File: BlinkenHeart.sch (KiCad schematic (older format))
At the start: 21 parts, among them IC1 ATTINY85-S, P1 CONN_01X06, SW1 SW_Push, SW2 SW_DPDT_x2

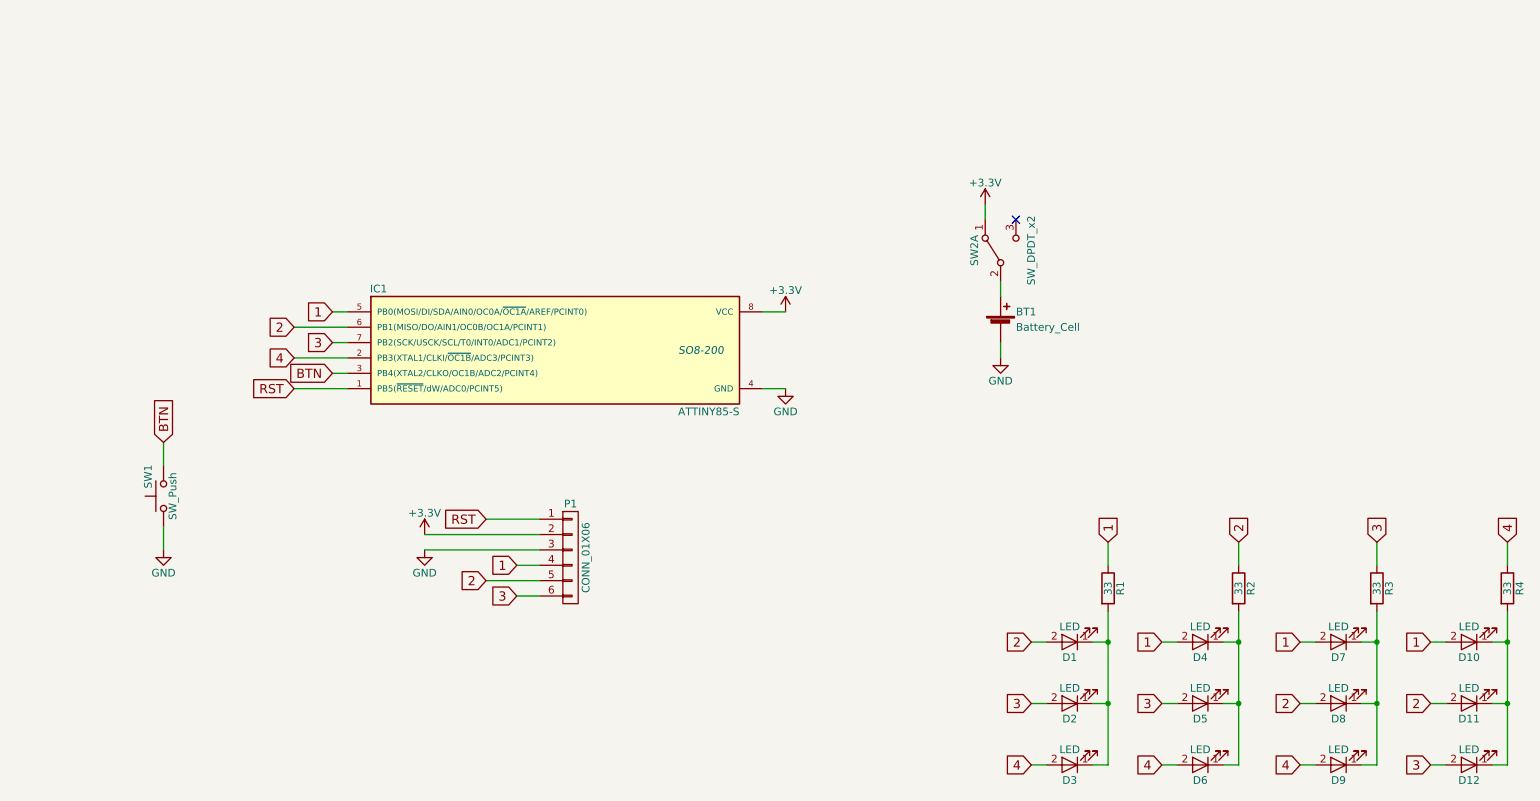
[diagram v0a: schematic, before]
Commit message: Did some refactoring of the schematic. Ordered the ICSP Pins. Added a VCC Capacitor and an Reset-Pull-Up-Resisor
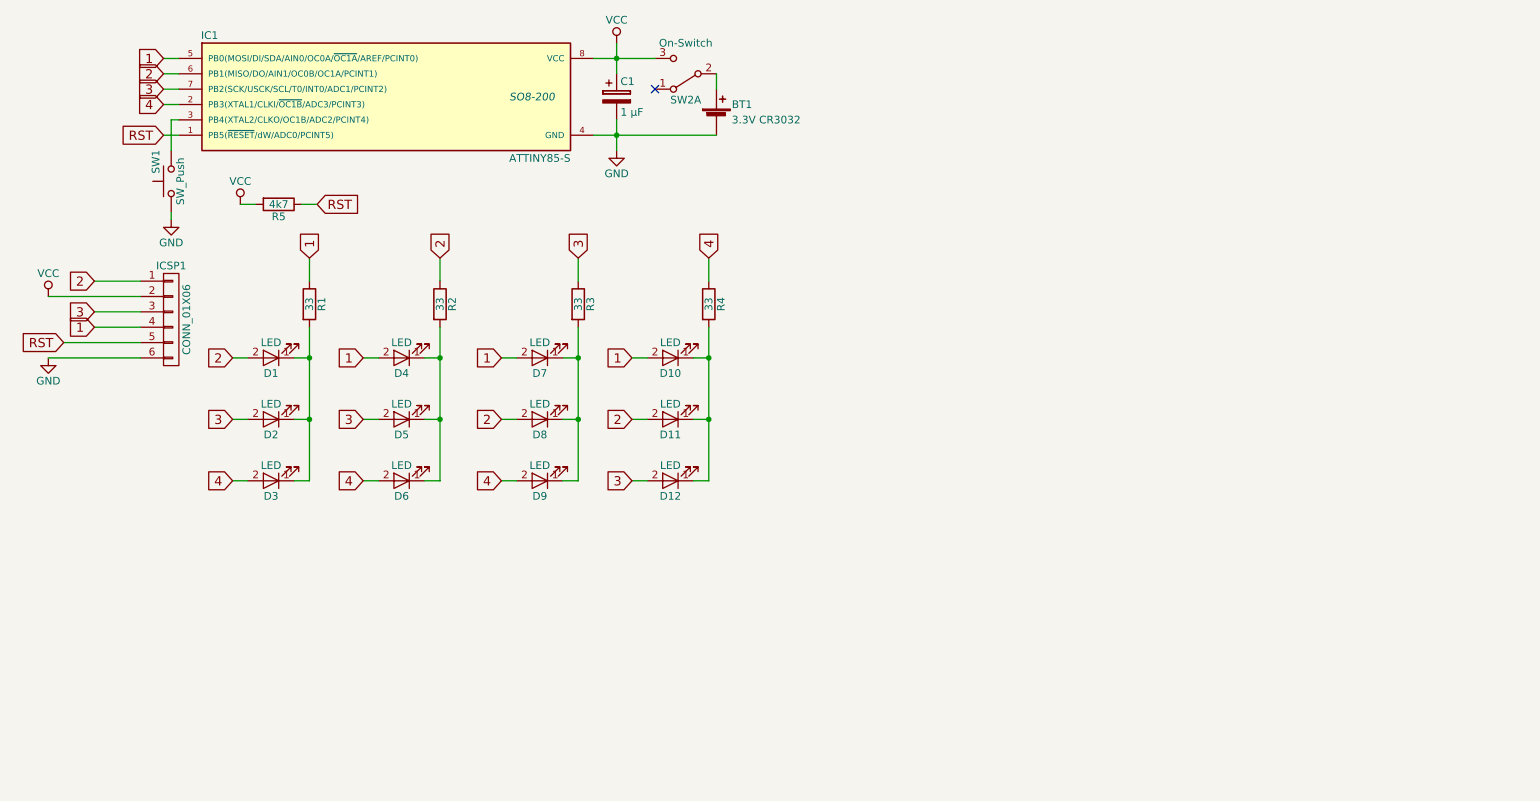
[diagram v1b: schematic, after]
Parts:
- added C1: 1 μF, symbol CP
- added R5: 4k7, symbol R
- BT1: value Battery_Cell -> 3.3V CR3032
- SW2: value SW_DPDT_x2 -> On-Switch
- renumbered P1 to ICSP1
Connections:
- net 2: now also ICSP1.1 (P1); no longer ICSP1.5 (P5)
- net 3: now also ICSP1.3 (P3); no longer ICSP1.6 (P6)
- net GND: now also ICSP1.6 (P6), C1.2; no longer ICSP1.3 (P3)
- net RST: now also ICSP1.5 (P5), R5.1; no longer ICSP1.1 (P1)
- net VCC: now reaches SW2.3 (C)
- net VCC: now also IC1.8 (VCC), ICSP1.2 (P2), C1.1, R5.2
- removed net +3V3: IC1.8 (VCC), ICSP1.2 (P2), SW2.1 (A)
- net BTN: no longer names the net of IC1.3 (PB4(XTAL2/CLKO/OC1B/ADC2/PCINT4)), SW1.2
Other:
- moved on the sheet: BT1, D1, D10, D11, D12, D2, D3, D4, D5, D6, D7, D8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

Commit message: assigned missing footprints
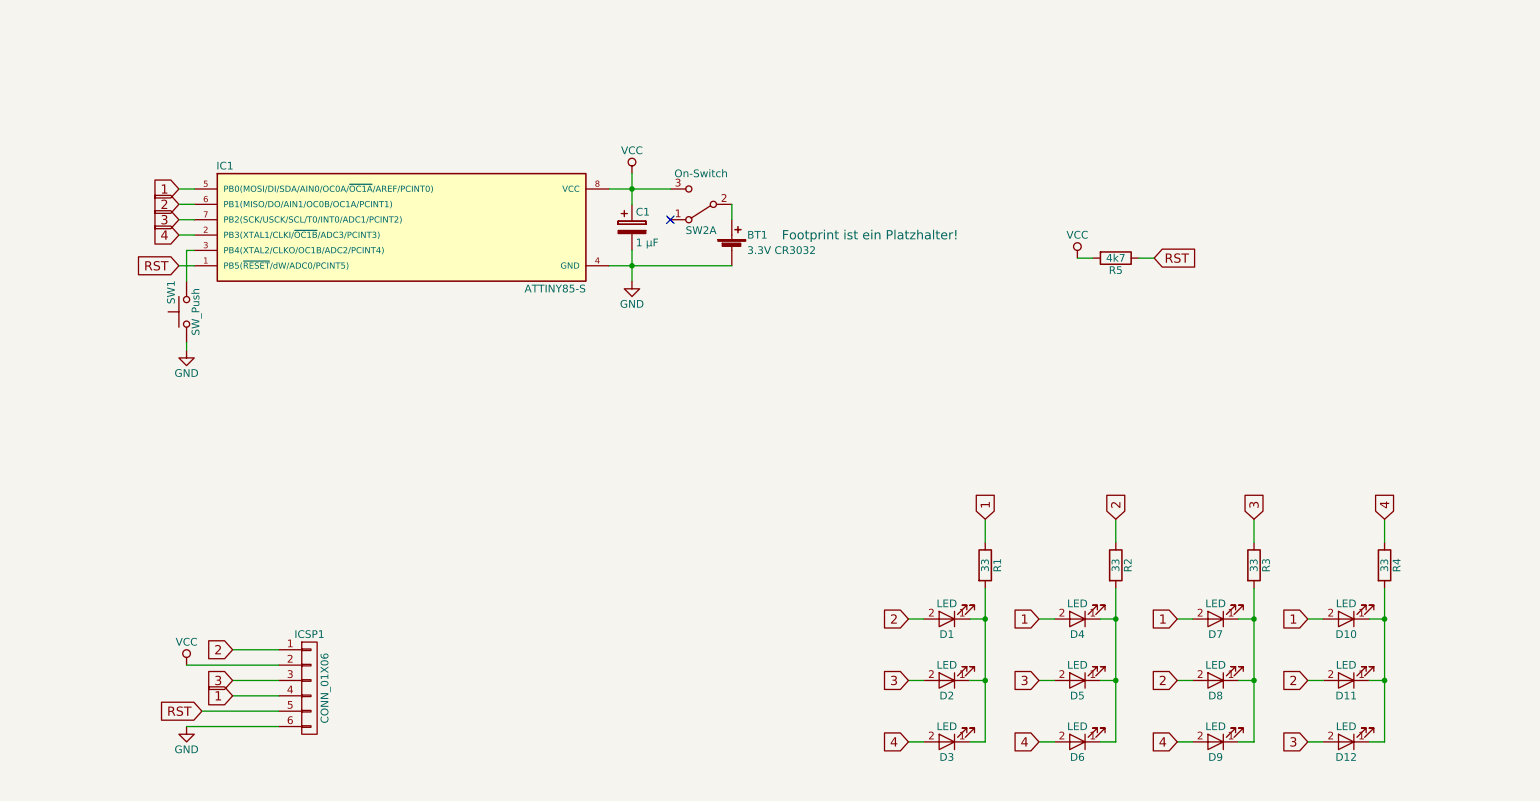
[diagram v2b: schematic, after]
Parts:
- BT1: footprint (none) -> CR3032-Holder:CR3032-Holder; Comment (none) -> Footprint ist ein Platzhalter!
- C1: footprint (none) -> Capacitors_SMD:C_1206; Component (none) -> C1206C105K3RACTU; Manufacturer (none) -> KEMET
- IC1: footprint SO8-200 -> Housings_SOIC:SOIC-8_3.9x4.9mm_Pitch1.27mm
- R5: footprint (none) -> Resistors_SMD:R_1206
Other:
- moved on the sheet: BT1, C1, D1, D10, D11, D12, D2, D3, D4, D5, D6, D7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

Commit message: finished border-cuts and routing
border-cuts is now a mathematicaly correct defined heart (thanks Mathias)
routing is complete, but needs some aesthetic changes
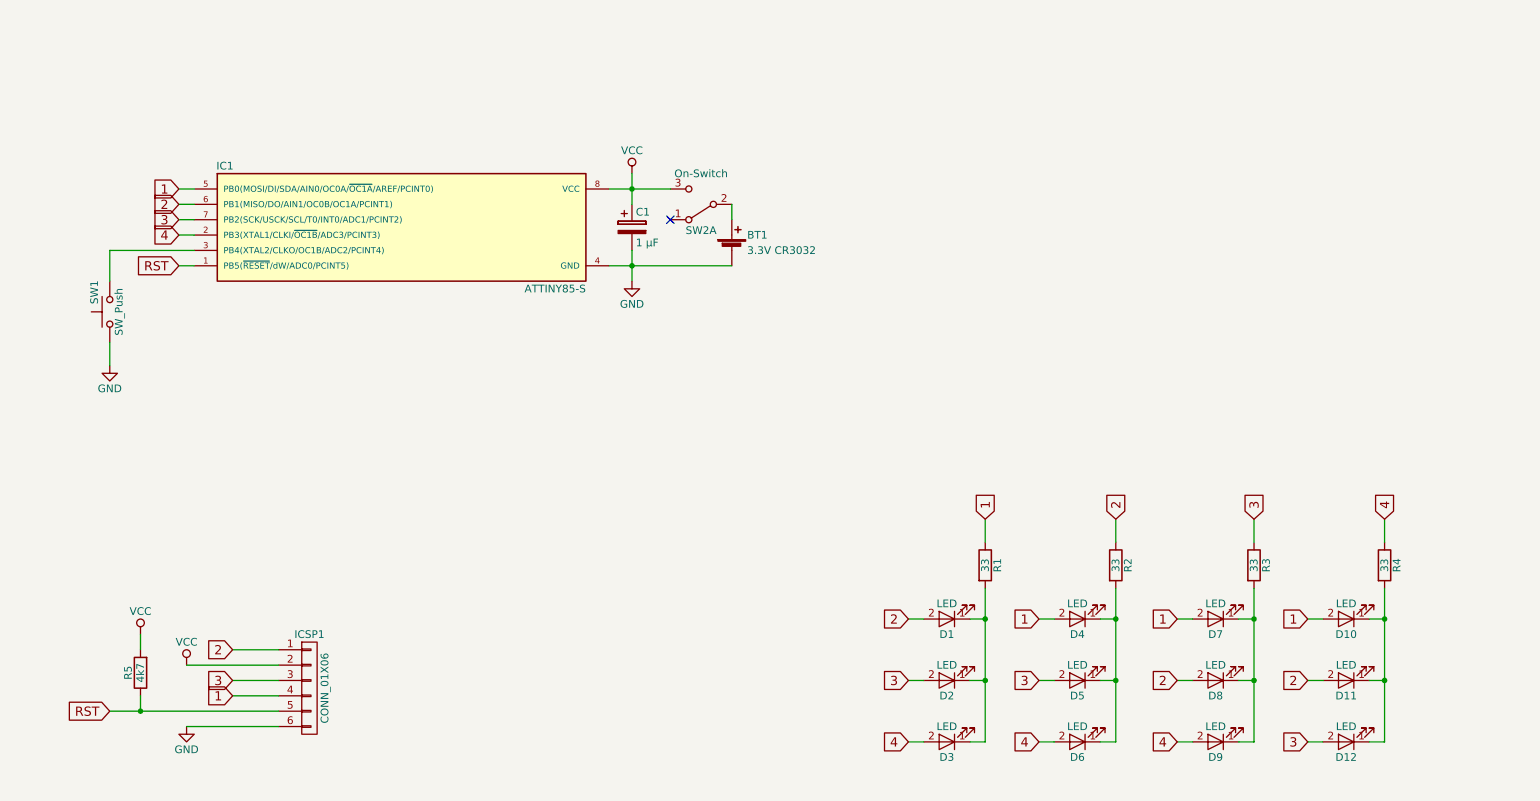
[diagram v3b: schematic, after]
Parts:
- BT1: Comment Footprint ist ein Platzhalter! -> (none)
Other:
- moved on the sheet: R5, SW1
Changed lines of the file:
@@
 F 2 "CR3032-Holder:CR3032-Holder" V 5350 2110 50  0001 C CNN
 F 3 "" V 5350 2110 50  0000 C CNN
-F 4 "Footprint ist ein Platzhalter!" H 6250 2150 60  0000 C CNN "Comment"
 	1    5350 2050
 	1    0    0    -1
@@
 Text GLabel 1750 2150 0    60   Input ~ 0
 RST
-Text GLabel 1900 5050 0    60   Input ~ 0
+Text GLabel 1300 5050 0    60   Input ~ 0
 RST
 $Comp
@@
 L SW_Push SW1
 U 1 1 58BB9CB1
-P 1800 2450
-F 0 "SW1" H 1850 2550 50  0000 L CNN
-F 1 "SW_Push" H 1800 2390 50  0000 C CNN
-F 2 "Buttons_Switches_SMD:SW_SPST_PTS645" H 1800 2650 50  0001 C CNN
-F 3 "" H 1800 2650 50  0000 C CNN
-	1    1800 2450
+P 1300 2450
+F 0 "SW1" H 1350 2550 50  0000 L CNN
+F 1 "SW_Push" H 1300 2390 50  0000 C CNN
+F 2 "Buttons_Switches_SMD:SW_SPST_PTS645" H 1300 2650 50  0001 C CNN
+F 3 "" H 1300 2650 50  0000 C CNN
+	1    1300 2450
 	0    -1   -1   0
 $EndComp
@@
 L GND #PWR03
 U 1 1 58BBA27D
-P 1800 2700
-F 0 "#PWR03" H 1800 2450 50  0001 C CNN
-F 1 "GND" H 1800 2550 50  0000 C CNN
-F 2 "" H 1800 2700 50  0000 C CNN
-F 3 "" H 1800 2700 50  0000 C CNN
-	1    1800 2700
+P 1300 2800
+F 0 "#PWR03" H 1300 2550 50  0001 C CNN
+F 1 "GND" H 1300 2650 50  0000 C CNN
+F 2 "" H 1300 2800 50  0000 C CNN
+F 3 "" H 1300 2800 50  0000 C CNN
+	1    1300 2800
 	1    0    0    -1
 $EndComp
@@
 	1750 2150 1850 2150
 Wire Wire Line
-	1800 2050 1800 2250
-Wire Wire Line
-	1800 2650 1800 2700
+	1300 2650 1300 2800
 Wire Wire Line
 	4550 1650 4950 1650
@@
 Connection ~ 4700 2150
 Wire Wire Line
-	1800 2050 1850 2050
-Wire Wire Line
-	1900 5050 2400 5050
+	1300 2050 1850 2050
 Wire Wire Line
 	2400 5150 1800 5150
@@
 L VCC #PWR06
 U 1 1 58C8935A
-P 7600 2100
-F 0 "#PWR06" H 7600 1950 50  0001 C CNN
-F 1 "VCC" H 7600 2250 50  0000 C CNN
-F 2 "" H 7600 2100 50  0001 C CNN
-F 3 "" H 7600 2100 50  0001 C CNN
-	1    7600 2100
-	1    0    0    -1
-$EndComp
-Text GLabel 8100 2100 2    60   Input ~ 0
-RST
+P 1500 4550
+F 0 "#PWR06" H 1500 4400 50  0001 C CNN
+F 1 "VCC" H 1500 4700 50  0000 C CNN
+F 2 "" H 1500 4550 50  0001 C CNN
+F 3 "" H 1500 4550 50  0001 C CNN
+	1    1500 4550
+	1    0    0    -1
+$EndComp
 $Comp
 L R R5
 U 1 1 58C897DF
-P 7850 2100
-F 0 "R5" V 7930 2100 50  0000 C CNN
-F 1 "4k7" V 7850 2100 50  0000 C CNN
-F 2 "Resistors_SMD:R_1206" V 7780 2100 50  0001 C CNN
-F 3 "" H 7850 2100 50  0001 C CNN
-	1    7850 2100
-	0    1    1    0
-$EndComp
-Wire Wire Line
-	7600 2100 7700 2100
-Wire Wire Line
-	8000 2100 8100 2100
+P 1500 4800
+F 0 "R5" V 1580 4800 50  0000 C CNN
+F 1 "4k7" V 1500 4800 50  0000 C CNN
+F 2 "Resistors_SMD:R_1206" V 1430 4800 50  0001 C CNN
+F 3 "" H 1500 4800 50  0001 C CNN
+	1    1500 4800
+	-1   0    0    1
+$EndComp
 $Comp
 L CP C1
@@
 	1    0    0    -1
 $EndComp
+Wire Wire Line
+	1300 2050 1300 2250
+Wire Wire Line
+	1300 5050 2400 5050
+Connection ~ 1500 5050
+Wire Wire Line
+	1500 5050 1500 4950
+Wire Wire Line
+	1500 4650 1500 4550
 $EndSCHEMATC

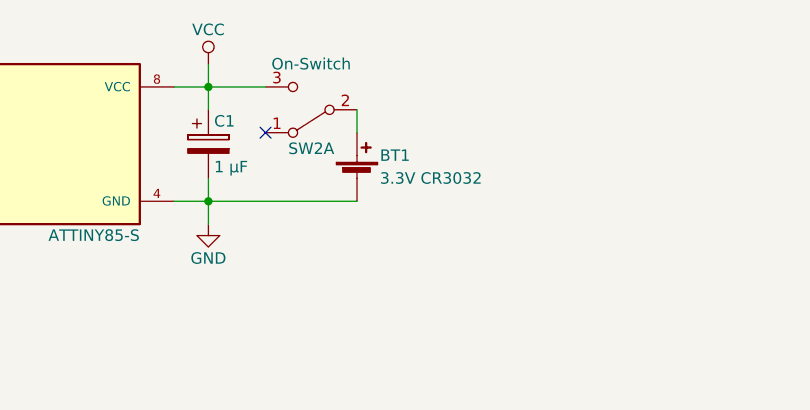
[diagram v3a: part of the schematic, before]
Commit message: Added some holes, fixed some other minor things. Also: Added a logo and did some rerouting
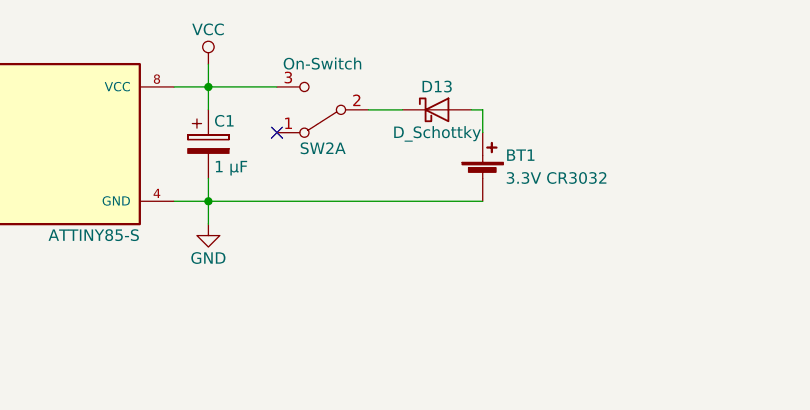
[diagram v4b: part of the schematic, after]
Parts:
- added D13: D_Schottky, symbol D_Schottky
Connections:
- net at BT1.1 (+): now also D13.2 (A); no longer SW2.2 (B)
- new net: D13.1 (K), SW2.2 (B)
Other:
- moved on the sheet: BT1, SW2A
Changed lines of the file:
@@
 L Battery_Cell BT1
 U 1 1 58BB3B7F
-P 5350 2050
-F 0 "BT1" H 5450 2150 50  0000 L CNN
-F 1 "3.3V CR3032" H 5450 2050 50  0000 L CNN
-F 2 "CR3032-Holder:CR3032-Holder" V 5350 2110 50  0001 C CNN
-F 3 "" V 5350 2110 50  0000 C CNN
-	1    5350 2050
+P 5900 2050
+F 0 "BT1" H 6000 2150 50  0000 L CNN
+F 1 "3.3V CR3032" H 6000 2050 50  0000 L CNN
+F 2 "CR3032-Holder:CR3032-Holder" V 5900 2110 50  0001 C CNN
+F 3 "" V 5900 2110 50  0000 C CNN
+	1    5900 2050
 	1    0    0    -1
 $EndComp
@@
 L SW_DPDT_x2 SW2
 U 1 1 58BB3E1D
-P 5150 1750
-F 0 "SW2" H 5150 1920 50  0000 C CNN
-F 1 "On-Switch" H 5150 1550 50  0000 C CNN
-F 2 "Soerens_Wunderschalter:Soerens_Wunderschalter" H 5150 1750 50  0001 C CNN
-F 3 "" H 5150 1750 50  0000 C CNN
-	1    5150 1750
+P 5200 1750
+F 0 "SW2" H 5200 1920 50  0000 C CNN
+F 1 "On-Switch" H 5200 1550 50  0000 C CNN
+F 2 "Soerens_Wunderschalter:Soerens_Wunderschalter" H 5200 1750 50  0001 C CNN
+F 3 "" H 5200 1750 50  0000 C CNN
+	1    5200 1750
 	-1   0    0    1
 $EndComp
@@
 	1    0    0    -1
 $EndComp
-NoConn ~ 4950 1850
-Wire Wire Line
-	1750 1650 1850 1650
-Wire Wire Line
-	1750 1750 1850 1750
-Wire Wire Line
-	1750 1850 1850 1850
-Wire Wire Line
-	1750 1950 1850 1950
-Wire Wire Line
-	7000 4250 7000 5250
-Wire Wire Line
-	7000 4450 6900 4450
-Wire Wire Line
-	7000 4850 6900 4850
-Connection ~ 7000 4450
-Wire Wire Line
-	7000 5250 6900 5250
-Connection ~ 7000 4850
-Wire Wire Line
-	6500 4450 6600 4450
-Wire Wire Line
-	6500 4850 6600 4850
-Wire Wire Line
-	6500 5250 6600 5250
-Wire Wire Line
-	7000 3950 7000 3800
-Wire Wire Line
-	7850 4250 7850 5250
-Wire Wire Line
-	7850 4450 7750 4450
-Wire Wire Line
-	7850 4850 7750 4850
-Connection ~ 7850 4450
-Wire Wire Line
-	7850 5250 7750 5250
-Connection ~ 7850 4850
-Wire Wire Line
-	7350 4450 7450 4450
-Wire Wire Line
-	7350 4850 7450 4850
-Wire Wire Line
-	7350 5250 7450 5250
-Wire Wire Line
-	7850 3950 7850 3800
-Wire Wire Line
-	8750 4250 8750 5250
-Wire Wire Line
-	8750 4450 8650 4450
-Wire Wire Line
-	8750 4850 8650 4850
-Connection ~ 8750 4450
-Wire Wire Line
-	8750 5250 8650 5250
-Connection ~ 8750 4850
-Wire Wire Line
-	8250 4450 8350 4450
-Wire Wire Line
-	8250 4850 8350 4850
-Wire Wire Line
-	8250 5250 8350 5250
-Wire Wire Line
-	8750 3950 8750 3800
-Wire Wire Line
-	9600 4250 9600 5250
-Wire Wire Line
-	9600 4450 9500 4450
-Wire Wire Line
-	9600 4850 9500 4850
-Connection ~ 9600 4450
-Wire Wire Line
-	9600 5250 9500 5250
-Connection ~ 9600 4850
-Wire Wire Line
-	9100 4450 9200 4450
-Wire Wire Line
-	9100 4850 9200 4850
-Wire Wire Line
-	9100 5250 9200 5250
-Wire Wire Line
-	9600 3950 9600 3800
-Wire Wire Line
-	1750 2150 1850 2150
-Wire Wire Line
-	1300 2650 1300 2800
-Wire Wire Line
-	4550 1650 4950 1650
-Wire Wire Line
-	4550 2150 5350 2150
-Wire Wire Line
-	4700 2050 4700 2250
-Connection ~ 4700 2150
-Wire Wire Line
-	1300 2050 1850 2050
-Wire Wire Line
-	2400 5150 1800 5150
-Wire Wire Line
-	2100 4850 2400 4850
-Wire Wire Line
-	2100 4650 2400 4650
-Wire Wire Line
-	2100 4950 2400 4950
-Wire Wire Line
-	5350 1750 5350 1850
+NoConn ~ 5000 1850
 $Comp
 L VCC #PWR04
@@
 	1    0    0    -1
 $EndComp
-Wire Wire Line
-	4700 1550 4700 1750
-Connection ~ 4700 1650
 $Comp
 L VCC #PWR05
@@
 	1    0    0    -1
 $EndComp
-Wire Wire Line
-	1800 4750 2400 4750
 $Comp
 L VCC #PWR06
@@
 	1    0    0    -1
 $EndComp
+$Comp
+L D_Schottky D13
+U 1 1 59135501
+P 5700 1750
+F 0 "D13" H 5700 1850 50  0000 C CNN
+F 1 "D_Schottky" H 5700 1650 50  0000 C CNN
+F 2 "" H 5700 1750 50  0001 C CNN
+F 3 "" H 5700 1750 50  0001 C CNN
+	1    5700 1750
+	1    0    0    -1
+$EndComp
+Wire Wire Line
+	1750 1650 1850 1650
+Wire Wire Line
+	1750 1750 1850 1750
+Wire Wire Line
+	1750 1850 1850 1850
+Wire Wire Line
+	1750 1950 1850 1950
+Wire Wire Line
+	7000 4250 7000 5250
+Wire Wire Line
+	7000 4450 6900 4450
+Wire Wire Line
+	7000 4850 6900 4850
+Connection ~ 7000 4450
+Wire Wire Line
+	7000 5250 6900 5250
+Connection ~ 7000 4850
+Wire Wire Line
+	6500 4450 6600 4450
+Wire Wire Line
+	6500 4850 6600 4850
+Wire Wire Line
+	6500 5250 6600 5250
+Wire Wire Line
+	7000 3950 7000 3800
+Wire Wire Line
+	7850 4250 7850 5250
+Wire Wire Line
+	7850 4450 7750 4450
+Wire Wire Line
+	7850 4850 7750 4850
+Connection ~ 7850 4450
+Wire Wire Line
+	7850 5250 7750 5250
+Connection ~ 7850 4850
+Wire Wire Line
+	7350 4450 7450 4450
+Wire Wire Line
+	7350 4850 7450 4850
+Wire Wire Line
+	7350 5250 7450 5250
+Wire Wire Line
+	7850 3950 7850 3800
+Wire Wire Line
+	8750 4250 8750 5250
+Wire Wire Line
+	8750 4450 8650 4450
+Wire Wire Line
+	8750 4850 8650 4850
+Connection ~ 8750 4450
+Wire Wire Line
+	8750 5250 8650 5250
+Connection ~ 8750 4850
+Wire Wire Line
+	8250 4450 8350 4450
+Wire Wire Line
+	8250 4850 8350 4850
+Wire Wire Line
+	8250 5250 8350 5250
+Wire Wire Line
+	8750 3950 8750 3800
+Wire Wire Line
+	9600 4250 9600 5250
+Wire Wire Line
+	9600 4450 9500 4450
+Wire Wire Line
+	9600 4850 9500 4850
+Connection ~ 9600 4450
+Wire Wire Line
+	9600 5250 9500 5250
+Connection ~ 9600 4850
+Wire Wire Line
+	9100 4450 9200 4450
+Wire Wire Line
+	9100 4850 9200 4850
+Wire Wire Line
+	9100 5250 9200 5250
+Wire Wire Line
+	9600 3950 9600 3800
+Wire Wire Line
+	1750 2150 1850 2150
+Wire Wire Line
+	1300 2650 1300 2800
+Wire Wire Line
+	4550 2150 5900 2150
+Wire Wire Line
+	4700 2050 4700 2250
+Connection ~ 4700 2150
+Wire Wire Line
+	1300 2050 1850 2050
+Wire Wire Line
+	2400 5150 1800 5150
+Wire Wire Line
+	2100 4850 2400 4850
+Wire Wire Line
+	2100 4650 2400 4650
+Wire Wire Line
+	2100 4950 2400 4950
+Wire Wire Line
+	4700 1550 4700 1750
+Connection ~ 4700 1650
+Wire Wire Line
+	1800 4750 2400 4750
 Wire Wire Line
 	1300 2050 1300 2250
@@
 Wire Wire Line
 	1500 4650 1500 4550
+Wire Wire Line
+	4550 1650 5000 1650
+Wire Wire Line
+	5400 1750 5550 1750
+Wire Wire Line
+	5850 1750 5900 1750
+Wire Wire Line
+	5900 1750 5900 1850
 $EndSCHEMATC
